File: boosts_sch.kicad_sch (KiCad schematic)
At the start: 42 parts, among them IC1 AP2205-W5-7, IC2 AP2205-W5-7, IC3 TPS61089RNRR, IC4 TPS61089RNRR

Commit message: Take 3
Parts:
- added C54: 22uF, Capacitor_SMD:C_0805_2012Metric, symbol Device:C_Small
- added R62 (x2): 10K, Resistor_SMD:R_0402_1005Metric, symbol Device:R_Small
- C57: footprint Capacitor_SMD:C_0805_2012Metric -> Capacitor_SMD:C_0402_1005Metric
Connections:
- net +3V3: now also R62.2, R62.2
- net GND: now also C54.2
- net LDO12V_IN: now also C54.1
- net at C55.1, IC4.2 (VCC): no longer IC4.7 (EN)
- net at C53.1, IC3.2 (VCC): no longer IC3.7 (EN)
- new net: IC4.7 (EN), R62.1
- new net: IC3.7 (EN), R62.1

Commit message: more changes
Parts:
- added R107: 492k, Resistor_SMD:R_0402_1005Metric, symbol Device:R_Small
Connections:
- net 12V: now also R107.2
- net at IC2.4 (ADJ/NC), R102.2: now also R107.1
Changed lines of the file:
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@@
 	)
 	(junction
+		(at 217.932 32.512)
+		(diameter 0)
+		(color 0 0 0 0)
+	)
+	(junction
+		(at 217.932 37.592)
+		(diameter 0)
+		(color 0 0 0 0)
+	)
+	(junction
 		(at 250.952 45.212)
 		(diameter 0)
@@
 	(wire
 		(pts
+			(xy 217.932 37.592) (xy 220.472 37.592)
+		)
+		(stroke
+			(width 0)
+			(type default)
+		)
+	)
+	(wire
+		(pts
 			(xy 135.382 68.072) (xy 135.382 69.342)
 		)
@@
 	(wire
 		(pts
-			(xy 215.392 37.592) (xy 220.472 37.592)
+			(xy 215.392 37.592) (xy 217.932 37.592)
 		)
 		(stroke
@@
 					(unit 1)
 				)
+			)
+		)
+	)
+	(symbol
+		(lib_id "Device:R_Small")
+		(at 217.932 35.052 0)
+		(unit 1)
+		(exclude_from_sim no)
+		(in_bom yes)
+		(on_board yes)
+		(dnp no)
+		(fields_autoplaced yes)
+		(property "Reference" "R107"
+			(at 215.392 35.687 0)
+			(effects
+				(font
+					(size 1.27 1.27)
+				)
+				(justify right)
+			)
+		)
+		(property "Value" "492k"
+			(at 215.392 33.147 0)
+			(effects
+				(font
+					(size 1.27 1.27)
+				)
+				(justify right)
+			)
+		)
+		(property "Footprint" "Resistor_SMD:R_0402_1005Metric"
+			(at 217.932 35.052 0)
+			(effects
+				(font
+					(size 1.27 1.27)
+				)
+				(hide yes)
+			)
+		)
+		(property "Datasheet" "~"
+			(at 217.932 35.052 0)
+			(effects
+				(font
+					(size 1.27 1.27)
+				)
+				(hide yes)
+			)
+		)
+		(property "Description" ""
+			(at 217.932 35.052 0)
+			(effects
+				(font
+					(size 1.27 1.27)
+				)
+				(hide yes)
+			)
+		)
+		(pin "1"
+		)
+		(pin "2"
+		)
+		(instances
+			(project "Ricardo-Stark"
+				(path "/7db990e4-92e1-4f99-b4d2-435bbec1ba83/df24f951-9014-423f-941d-dec7c0c4c8db"
+					(reference "R107")
+					(unit 1)
+				)

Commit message: changed boost out
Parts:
- R65: value 900k -> 976k
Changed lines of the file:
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@@
 		(fields_autoplaced yes)
 		(property "Reference" "R65"
-			(at 205.74 117.602 0)
+			(at 205.74 117.6019 0)
 			(effects
 				(font
@@
 			)
 		)
-		(property "Value" "900k"
-			(at 205.74 120.142 0)
+		(property "Value" "976k"
+			(at 205.74 120.1419 0)
 			(effects
 				(font

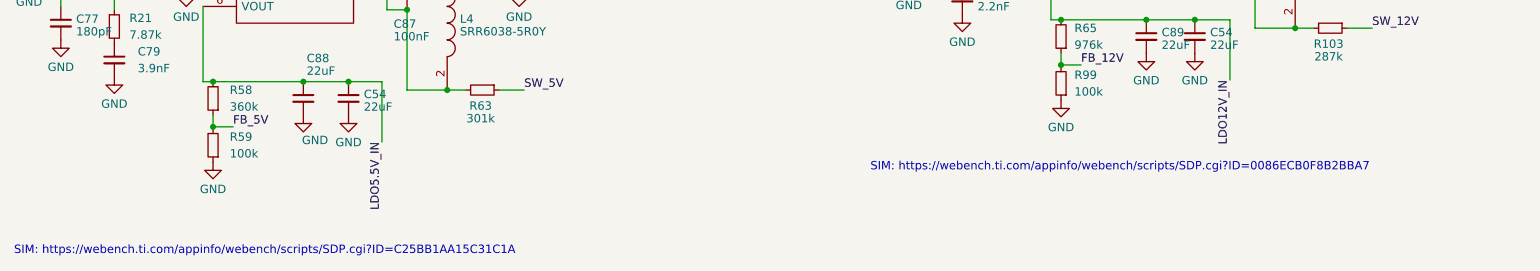
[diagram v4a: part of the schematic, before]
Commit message: tcmt1109 instead of ltv
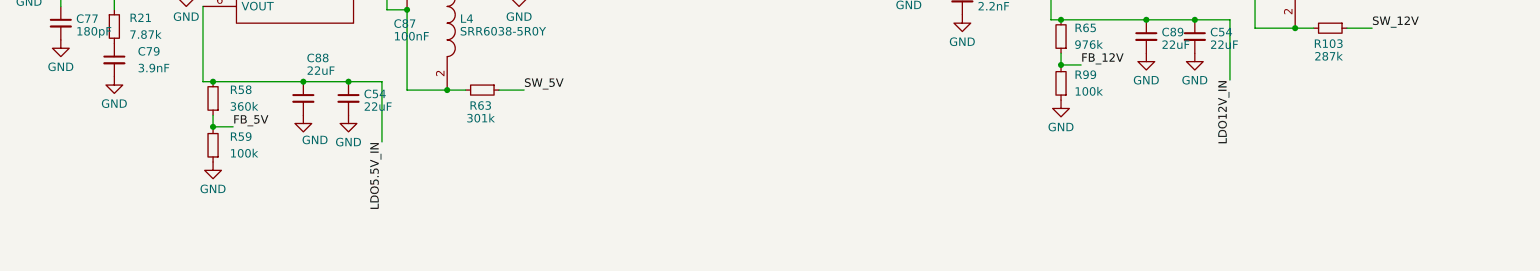
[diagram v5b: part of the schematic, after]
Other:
- note removed: "SIM: https://webench.ti.com/appinfo/webench/scripts/SDP.cgi?ID=0086ECB0F8B2BBA7"
- note removed: "SIM: https://webench.ti.com/appinfo/webench/scripts/SDP.cgi?ID=C25BB1AA15C31C1A"
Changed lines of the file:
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@@
-		)
-	)
-	(text "SIM: https://webench.ti.com/appinfo/webench/scripts/SDP.cgi?ID=C25BB1AA15C31C1A"
-		(exclude_from_sim no)
-		(at 44.704 152.146 0)
-		(effects
-			(font
-				(size 1.27 1.27)
-			)
-			(justify left bottom)
-		)
-	)
-	(text "SIM: https://webench.ti.com/appinfo/webench/scripts/SDP.cgi?ID=0086ECB0F8B2BBA7"
-		(exclude_from_sim no)
-		(at 174.752 139.446 0)
-		(effects
-			(font
-				(size 1.27 1.27)
-			)
-			(justify left bottom)
 		)
 	)

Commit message: Andrei review changes
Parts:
- R107: value 492k -> 360k
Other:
- note removed: "Vout"
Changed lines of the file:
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@@
 		)
 	)
-	(text "Vout"
-		(exclude_from_sim no)
-		(at 164.592 54.102 0)
-		(effects
-			(font
-				(size 1.27 1.27)
-			)
-			(justify left bottom)
-		)
-	)
 	(label "LDO5.5V_IN"
 		(at 135.382 68.072 180)
@@
 		(dnp no)
 		(property "Reference" "R64"
-			(at 187.2234 107.3063 0)
+			(at 193.548 106.934 0)
 			(effects
 				(font
@@
 		)
 		(property "Value" "18.7k"
-			(at 187.2234 109.2273 0)
+			(at 195.072 108.712 0)
 			(effects
 				(font
@@
 		(on_board yes)
 		(dnp no)
-		(fields_autoplaced yes)
 		(property "Reference" "R107"
-			(at 215.392 35.687 0)
+			(at 224.536 35.56 0)
 			(effects
 				(font
@@
 			)
 		)
-		(property "Value" "492k"
-			(at 215.392 33.147 0)
+		(property "Value" "360k"
+			(at 224.282 33.782 0)
 			(effects
 				(font
@@
 		(on_board yes)
 		(dnp no)
-		(fields_autoplaced yes)
 		(property "Reference" "C89"
-			(at 218.9861 118.2346 0)
+			(at 218.44 118.618 0)
 			(effects
 				(font
@@
 		)
 		(property "Value" "22uF"
-			(at 218.9861 120.1556 0)
+			(at 218.186 120.904 0)
 			(effects
 				(font
@@
 		(on_board yes)
 		(dnp no)
-		(fields_autoplaced yes)
 		(property "Reference" "C56"
-			(at 182.9181 106.8046 0)
+			(at 182.118 107.696 0)
 			(effects
 				(font
@@
 		)
 		(property "Value" "120pF"
-			(at 182.9181 108.7256 0)
+			(at 181.864 109.982 0)
 			(effects
 				(font
@@
 		(on_board yes)
 		(dnp no)
-		(fields_autoplaced yes)
 		(property "Reference" "C54"
-			(at 226.3521 118.2346 0)
+			(at 225.552 118.11 0)
 			(effects
 				(font
@@
 		)
 		(property "Value" "22uF"
-			(at 226.3521 120.1556 0)
+			(at 224.282 120.904 0)
 			(effects
 				(font

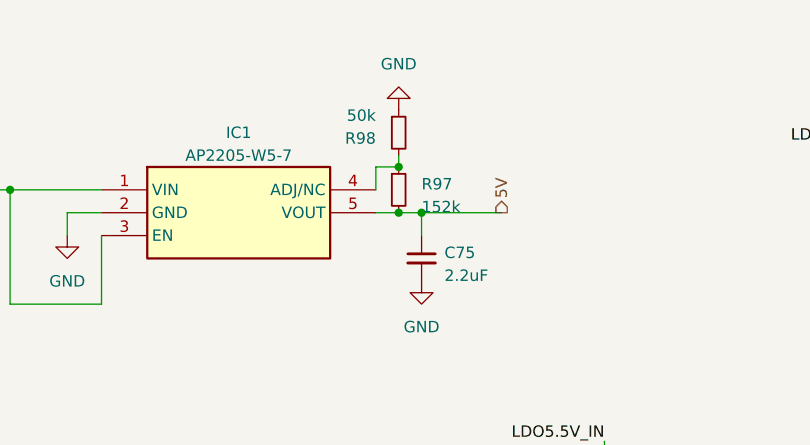
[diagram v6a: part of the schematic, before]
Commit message: LDO 5V resistor change
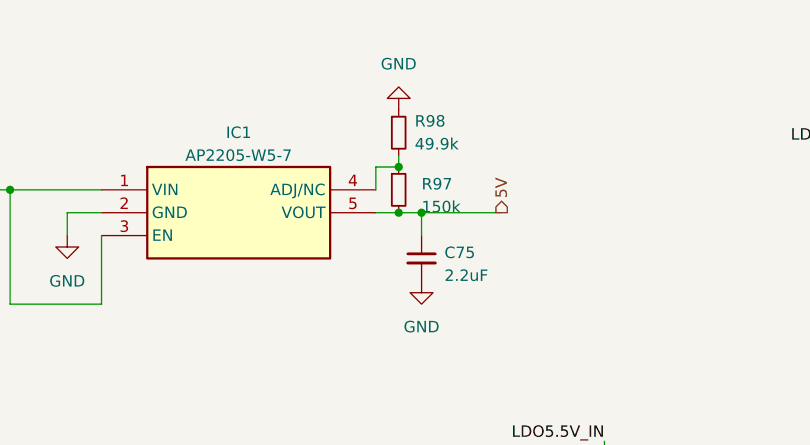
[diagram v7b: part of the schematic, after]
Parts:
- R97: value 152k -> 150k
- R98: value 50k -> 49.9k
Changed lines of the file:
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@@
 		(fields_autoplaced yes)
 		(property "Reference" "R98"
-			(at 109.982 34.417 0)
-			(effects
-				(font
-					(size 1.27 1.27)
-				)
-				(justify right)
-			)
-		)
-		(property "Value" "50k"
-			(at 109.982 31.877 0)
-			(effects
-				(font
-					(size 1.27 1.27)
-				)
-				(justify right)
+			(at 114.3 32.5119 0)
+			(effects
+				(font
+					(size 1.27 1.27)
+				)
+				(justify left)
+			)
+		)
+		(property "Value" "49.9k"
+			(at 114.3 35.0519 0)
+			(effects
+				(font
+					(size 1.27 1.27)
+				)
+				(justify left)
 			)
 		)
@@
 			)
 		)
-		(property "Value" "152k"
+		(property "Value" "150k"
 			(at 115.062 42.037 0)
 			(effects
